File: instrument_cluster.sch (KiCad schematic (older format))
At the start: 2 parts, among them J1 Conn_02x16_Top_Bottom, J2 Conn_02x16_Top_Bottom

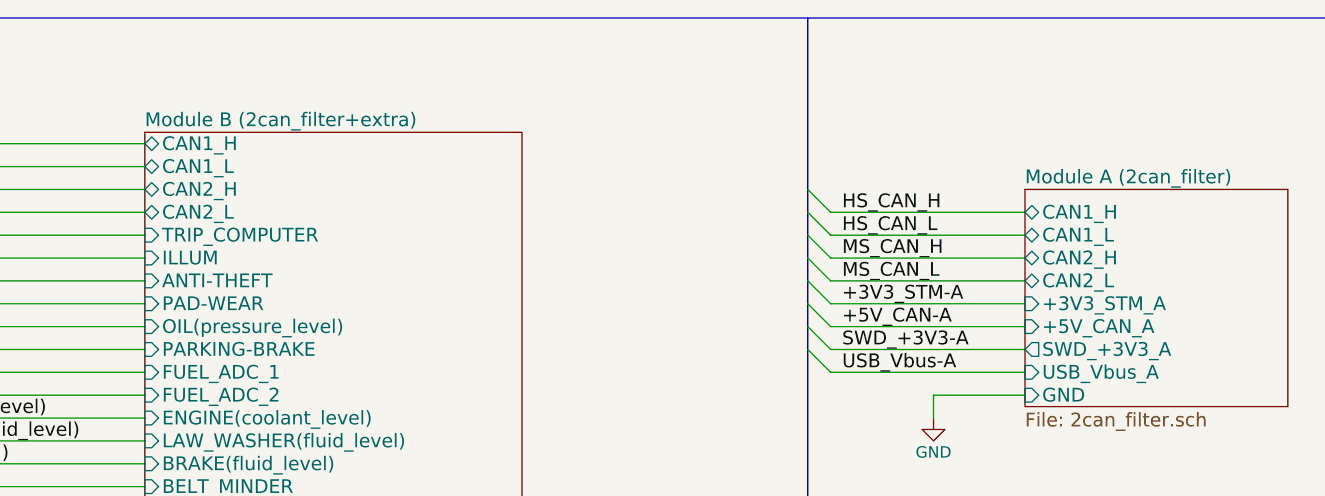
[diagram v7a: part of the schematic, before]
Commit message: fix CAN, swapped the stm->to->can connection in module B
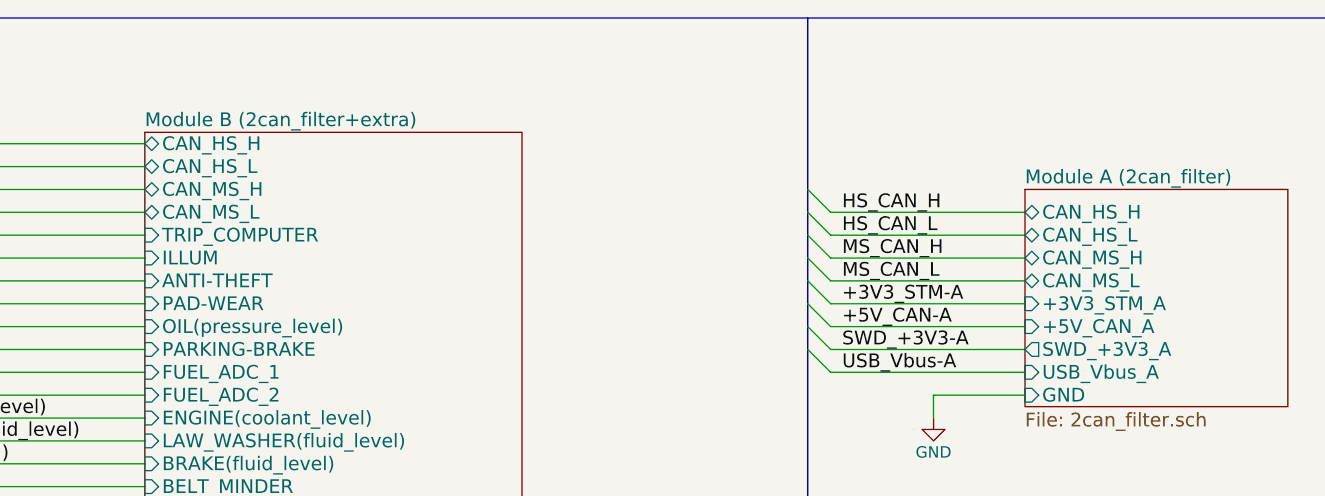
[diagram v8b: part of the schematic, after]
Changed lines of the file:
@@
 LIBS:valves
 LIBS:stm32
-LIBS:LM2596SX-5.0_NOPB
-LIBS:lm2575s-5
-LIBS:74HC4050D
-LIBS:54819-0572
+LIBS:zpkl
 LIBS:instrument_cluster-cache
 EELAYER 25 0
@@
 F0 "Module A (2can_filter)" 60
 F1 "2can_filter.sch" 60
-F2 "CAN1_H" B L 6200 1550 60
-F3 "CAN1_L" B L 6200 1650 60
-F4 "CAN2_H" B L 6200 1750 60
-F5 "CAN2_L" B L 6200 1850 60
+F2 "CAN_HS_H" B L 6200 1550 60
+F3 "CAN_HS_L" B L 6200 1650 60
+F4 "CAN_MS_H" B L 6200 1750 60
+F5 "CAN_MS_L" B L 6200 1850 60
 F6 "GND" I L 6200 2350 60
 F7 "USB_Vbus_A" I L 6200 2250 60
@@
 F2 "GND" I L 2350 3950 60
 F3 "USB_Vbus_B" O L 2350 3650 60
-F4 "CAN1_H" B L 2350 1250 60
-F5 "CAN1_L" B L 2350 1350 60
-F6 "CAN2_H" B L 2350 1450 60
-F7 "CAN2_L" B L 2350 1550 60
+F4 "CAN_HS_H" B L 2350 1250 60
+F5 "CAN_HS_L" B L 2350 1350 60
+F6 "CAN_MS_H" B L 2350 1450 60
+F7 "CAN_MS_L" B L 2350 1550 60
 F8 "TRIP_COMPUTER" I L 2350 1650 60
 F9 "ILLUM" I L 2350 1750 60
